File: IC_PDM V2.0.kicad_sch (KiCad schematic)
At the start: 43 parts, among them J1 RST, J10 Conn_01x04, J11 Conn_01x04, J12 Conn_01x04, J13 Conn_01x04, J14 Conn_01x04, J15 Conn_01x04, J16 Conn_01x02, J2 BSEL, J3 S03B-XASK-1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

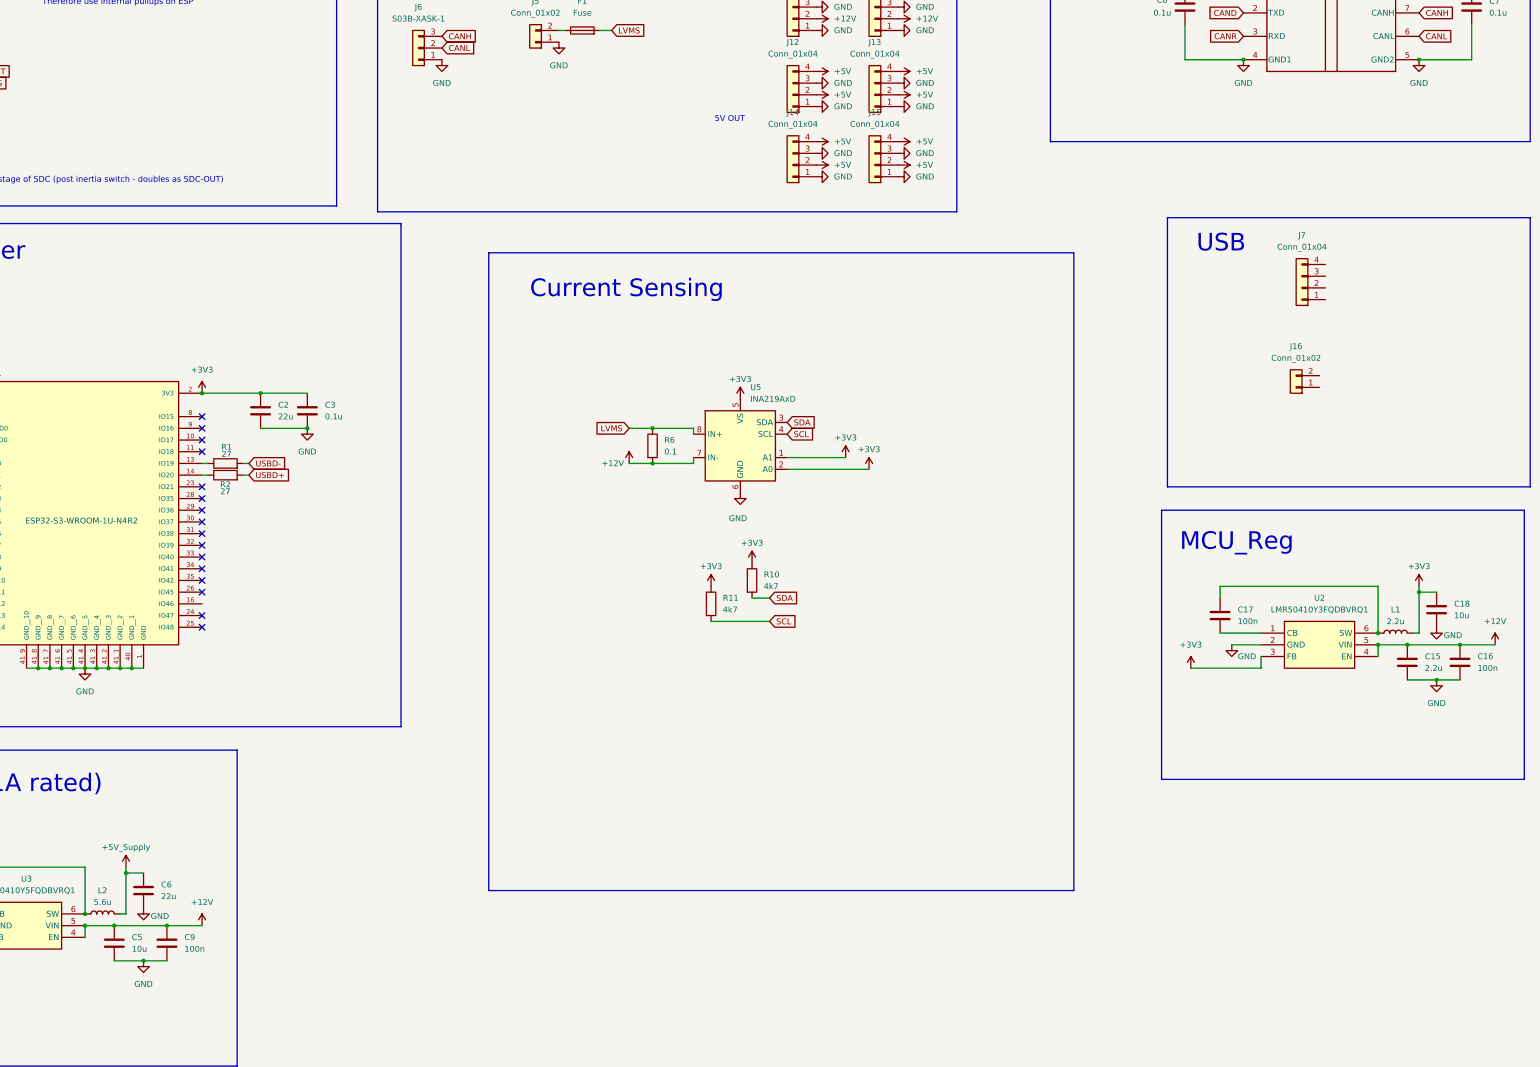
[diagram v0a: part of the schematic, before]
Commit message: Bosh
Routed PCB and fixed schematic
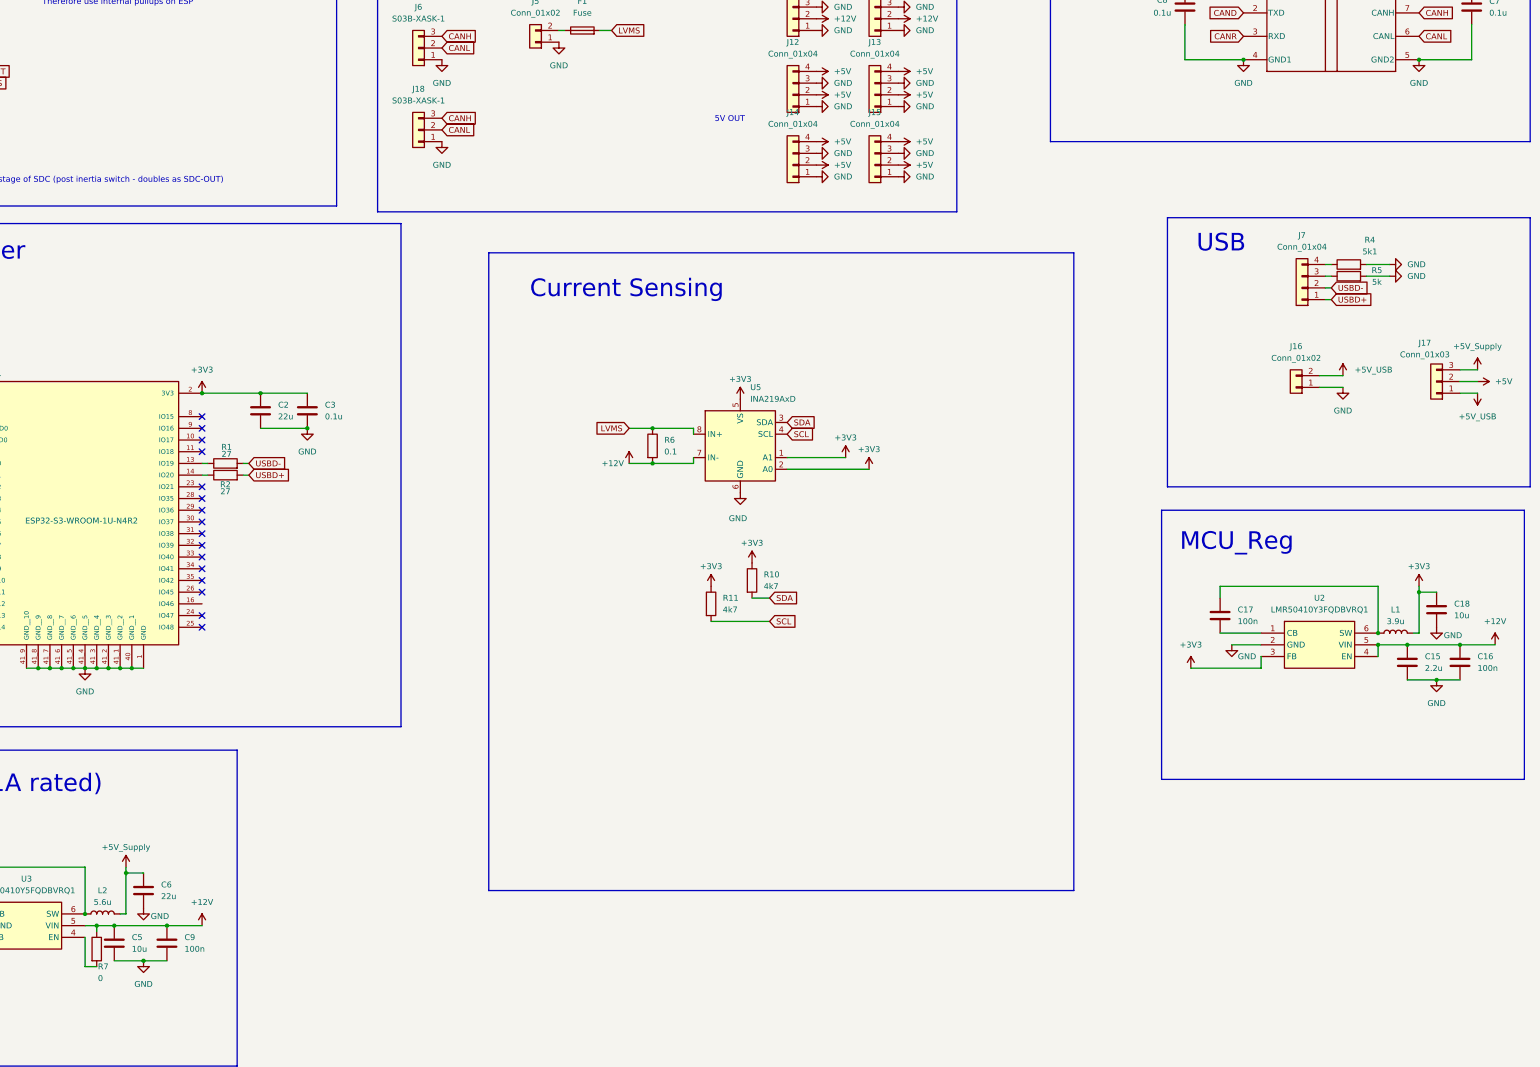
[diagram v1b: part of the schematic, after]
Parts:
- added J17: Conn_01x03, Connector_PinHeader_2.54mm:PinHeader_1x03_P2.54mm_Vertical, symbol Connector_Generic:Conn_01x03
- added J18: S03B-XASK-1, Connector_JST:JST_XA_S03B-XASK-1_1x03_P2.50mm_Horizontal, symbol Connector_Generic:Conn_01x03
- added R4: 5k1, Resistor_SMD:R_0603_1608Metric, symbol Device:R
- added R5: 5k, Resistor_SMD:R_0603_1608Metric, symbol Device:R
- added R7: 0, Resistor_SMD:R_0603_1608Metric, symbol Device:R
- C1, C15, C16, C17, C18, C2, C3, C4, C5, C6, C7, C8, C9: footprint Capacitor_SMD:C_0805_2012Metric_Pad1.18x1.45mm_HandSolder -> Capacitor_SMD:C_0603_1608Metric
- L1: value 2.2u -> 3.9u; footprint Inductor_SMD:L_0805_2012Metric_Pad1.15x1.40mm_HandSolder -> Inductor_SMD:L_0603_1608Metric
- L2: footprint Inductor_SMD:L_0805_2012Metric_Pad1.15x1.40mm_HandSolder -> Inductor_SMD:L_0603_1608Metric
- R1, R10, R11, R2, R3: footprint Resistor_SMD:R_0805_2012Metric_Pad1.20x1.40mm_HandSolder -> Resistor_SMD:R_0603_1608Metric
- R6: footprint Resistor_SMD:R_2512_6332Metric_Pad1.40x3.35mm_HandSolder -> Resistor_SMD:R_0603_1608Metric
- U1: footprint CustomFootprints:XCVR_ESP32-S3-WROOM-1U-N4R2 -> RF_Module:ESP32-S3-WROOM-1U
- U2, U3: footprint CustomFootprints:SOT95P280X145-6N -> Custom_MSM:Regulator_Switching_SOT-23-6
- U4: footprint CustomFootprints:DWV0008A-MFG -> customFootprints:DWV0008A-MFG
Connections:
- net +12V: now also R7.1; no longer U3.4 (EN)
- net +5V: now also J17.2 (Pin_2)
- net +5V_Supply: now also J17.3 (Pin_3)
- net CANH: now also J18.3 (Pin_3)
- net CANL: now also J18.2 (Pin_2)
- net GND: now also J16.1 (Pin_1), J18.1 (Pin_1), R4.2, R5.2
- net USBD+: now also J7.1 (Pin_1)
- net USBD-: now also J7.2 (Pin_2)
- net at J7.3 (Pin_3): now also R5.1
- net at J7.4 (Pin_4): now also R4.1
- net +5V_USB: now reaches J16.2 (Pin_2)
- net +5V_USB: now also J17.1 (Pin_1)
- new net: R7.2, U3.4 (EN)
